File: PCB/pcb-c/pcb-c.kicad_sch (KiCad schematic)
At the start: 37 parts, among them Q1 BC817, Q13 TPCA8120,L1Q, Q2 TPCA8120,L1Q, Q3 BC817, Q4 BC817, Q5 TPCA8120,L1Q, Q6 BC817, Q7 TPCA8120,L1Q, Q8 BC817, Q9 TPCA8120,L1Q

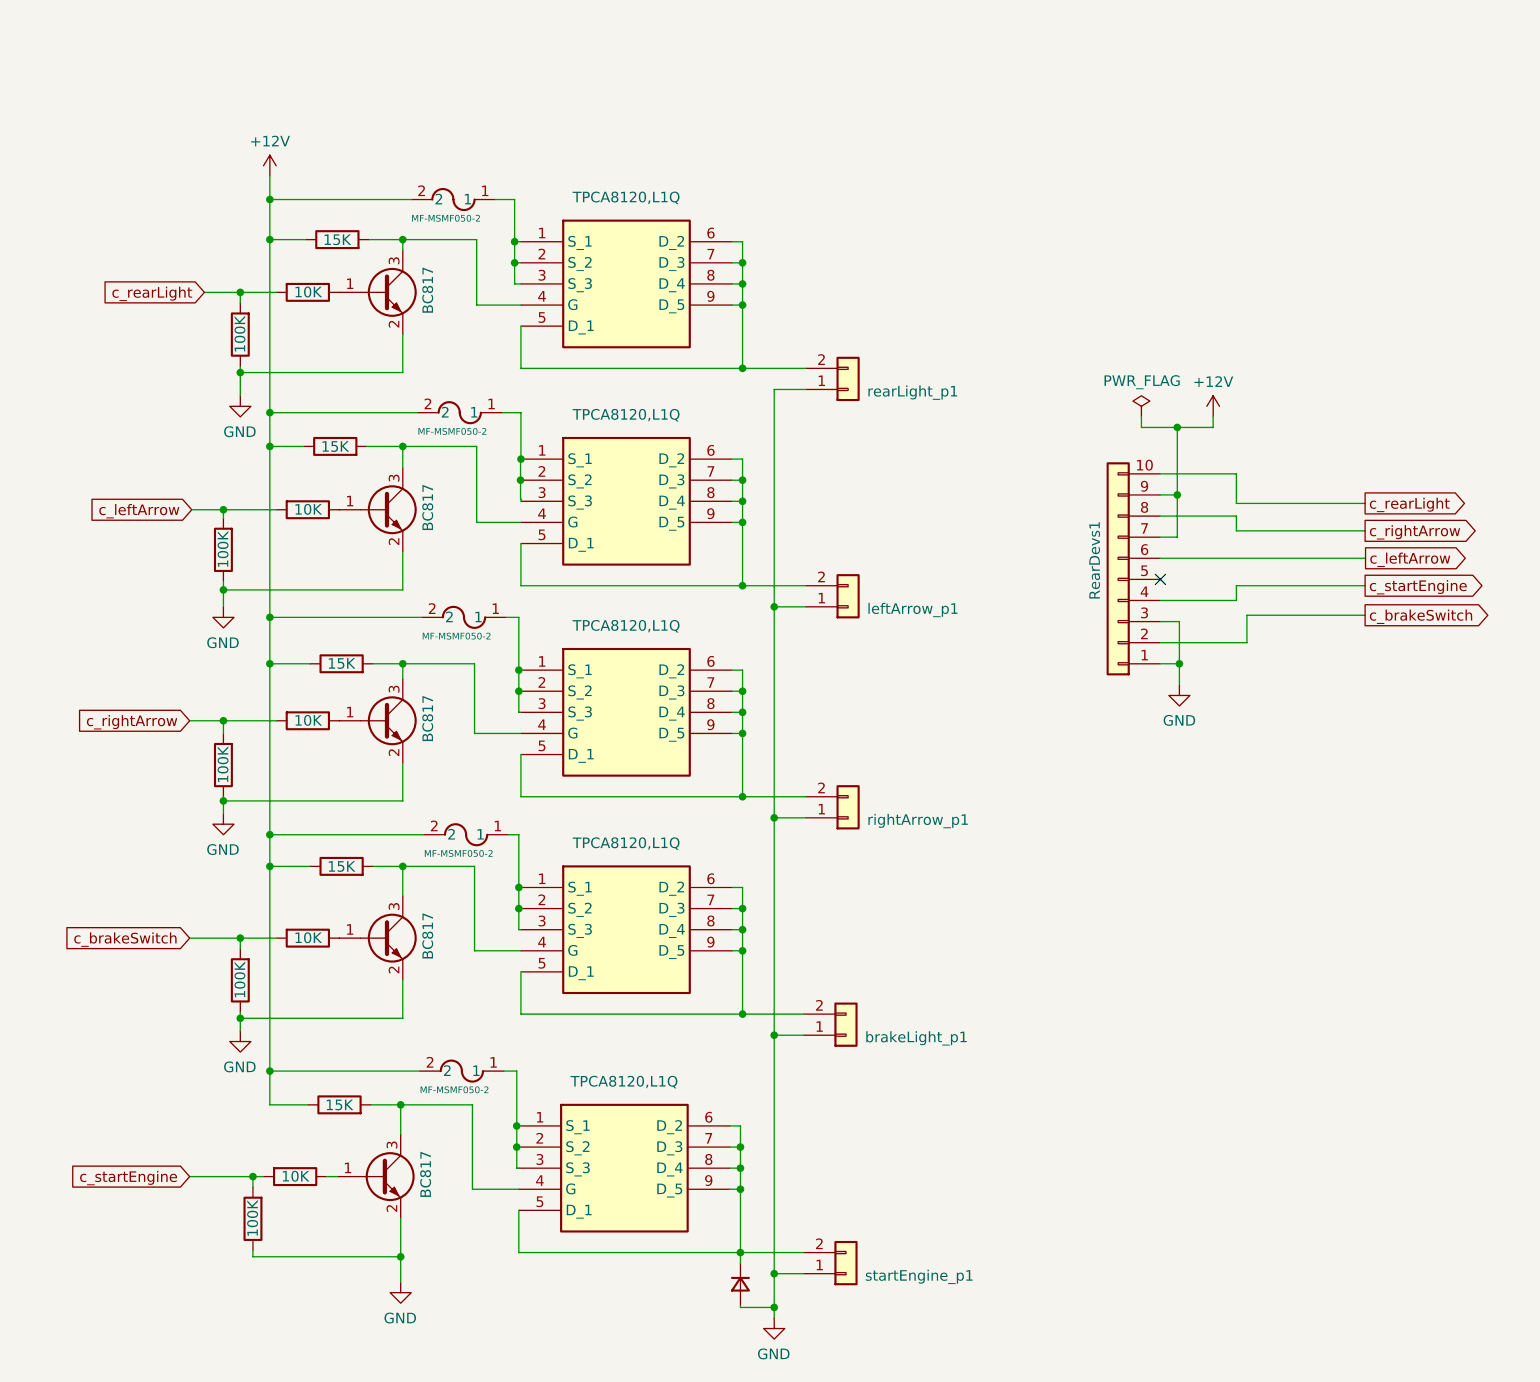
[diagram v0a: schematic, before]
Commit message: Floating FET's source pin fixed
The pin was in floating state when the associated fuse is temporary off
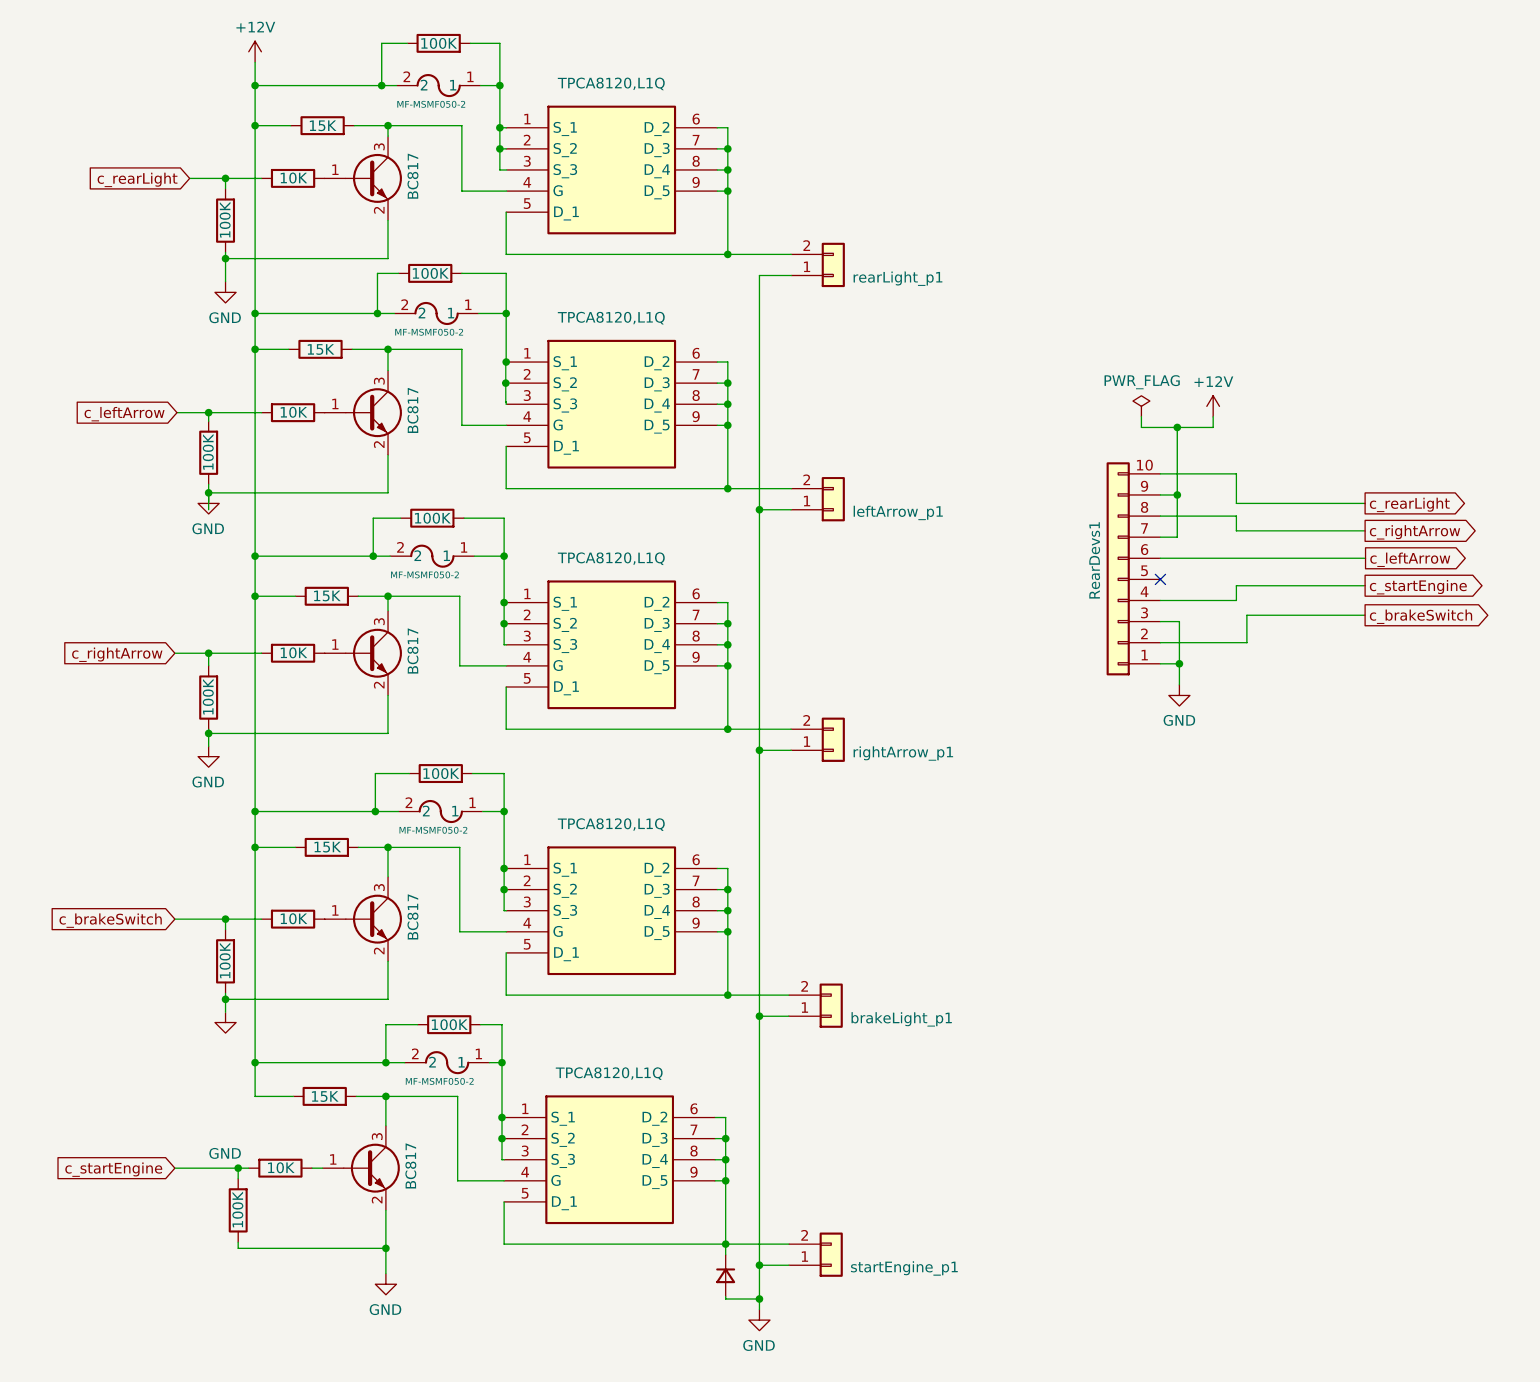
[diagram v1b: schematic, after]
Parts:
- added R11, R15, R19, R3, R6: 100K, Resistor_SMD:R_1206_3216Metric, symbol Device:R
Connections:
- net +12V: now also R11.1, R15.1, R19.1, R3.1, R6.1
- net at F3.1, Q13.1 (S_1), Q13.2 (S_2)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: now also R19.2
- net at F5.1, Q5.1 (S_1), Q5.2 (S_2)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: now also R3.2
- net at F4.1, Q7.1 (S_1), Q7.2 (S_2)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: now also R15.2
- net at F2.1, Q2.1 (S_1), Q2.2 (S_2)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: now also R6.2
- net at F1.1, Q9.1 (S_1), Q9.2 (S_2)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: now also R11.2
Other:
- moved on the sheet: brakeLight_p1, leftArrow_p1, rearLight_p1, rightArrow_p1, startEngine_p1
